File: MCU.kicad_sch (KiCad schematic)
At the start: 41 parts, among them IC9 ATSAMD21G18A-MF, J10 SAMTEC_SSW-106-01-L-S, J7 SAMTEC_SSW-108-01-G-S, J8 SAMTEC_SSW-110-01-G-S, J9 SAMTEC_SSW-108-01-G-S, Q1 XTAL_32.768KHZ_ABRACON_ABS09-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

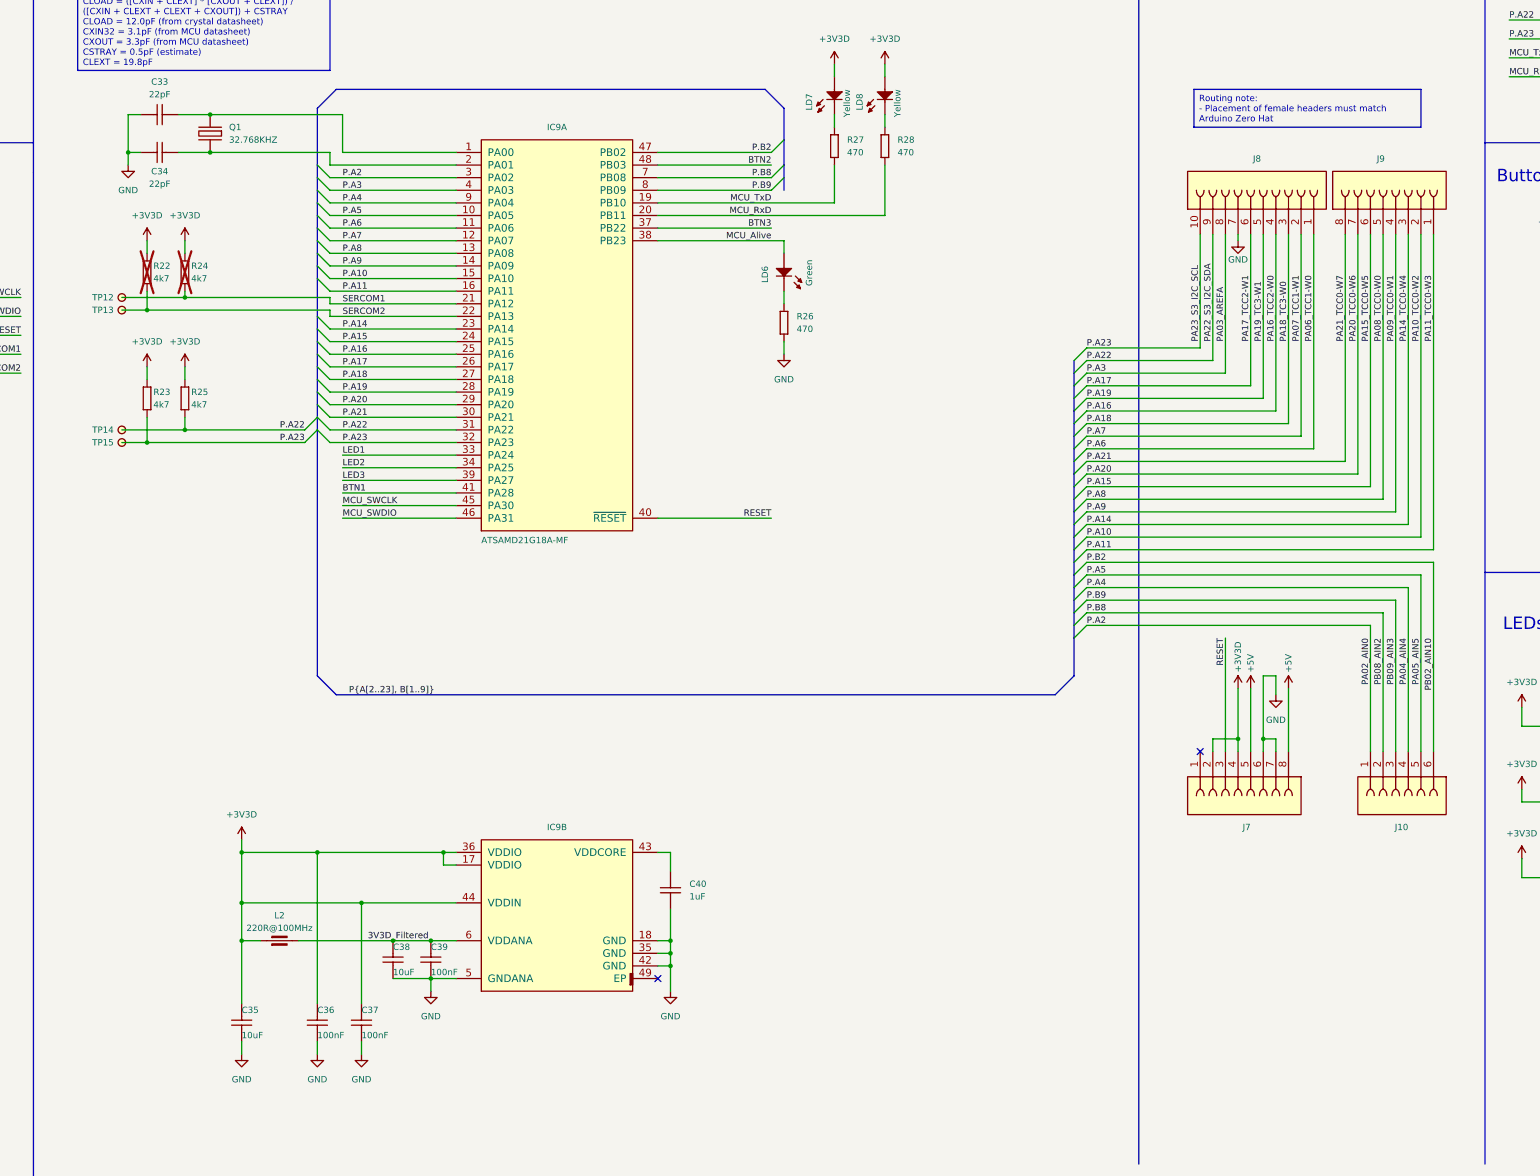
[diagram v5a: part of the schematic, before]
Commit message: Fixed reset circuits, removed 1V2 LED, fixing 2V5 circuit, added pullups to FPGA I2C, moved PSU TPs and JMPrs, replaced OSC2, removed ADC, added 2232 DTR, removed PSU seq TPs, replaced 2V5 LED res
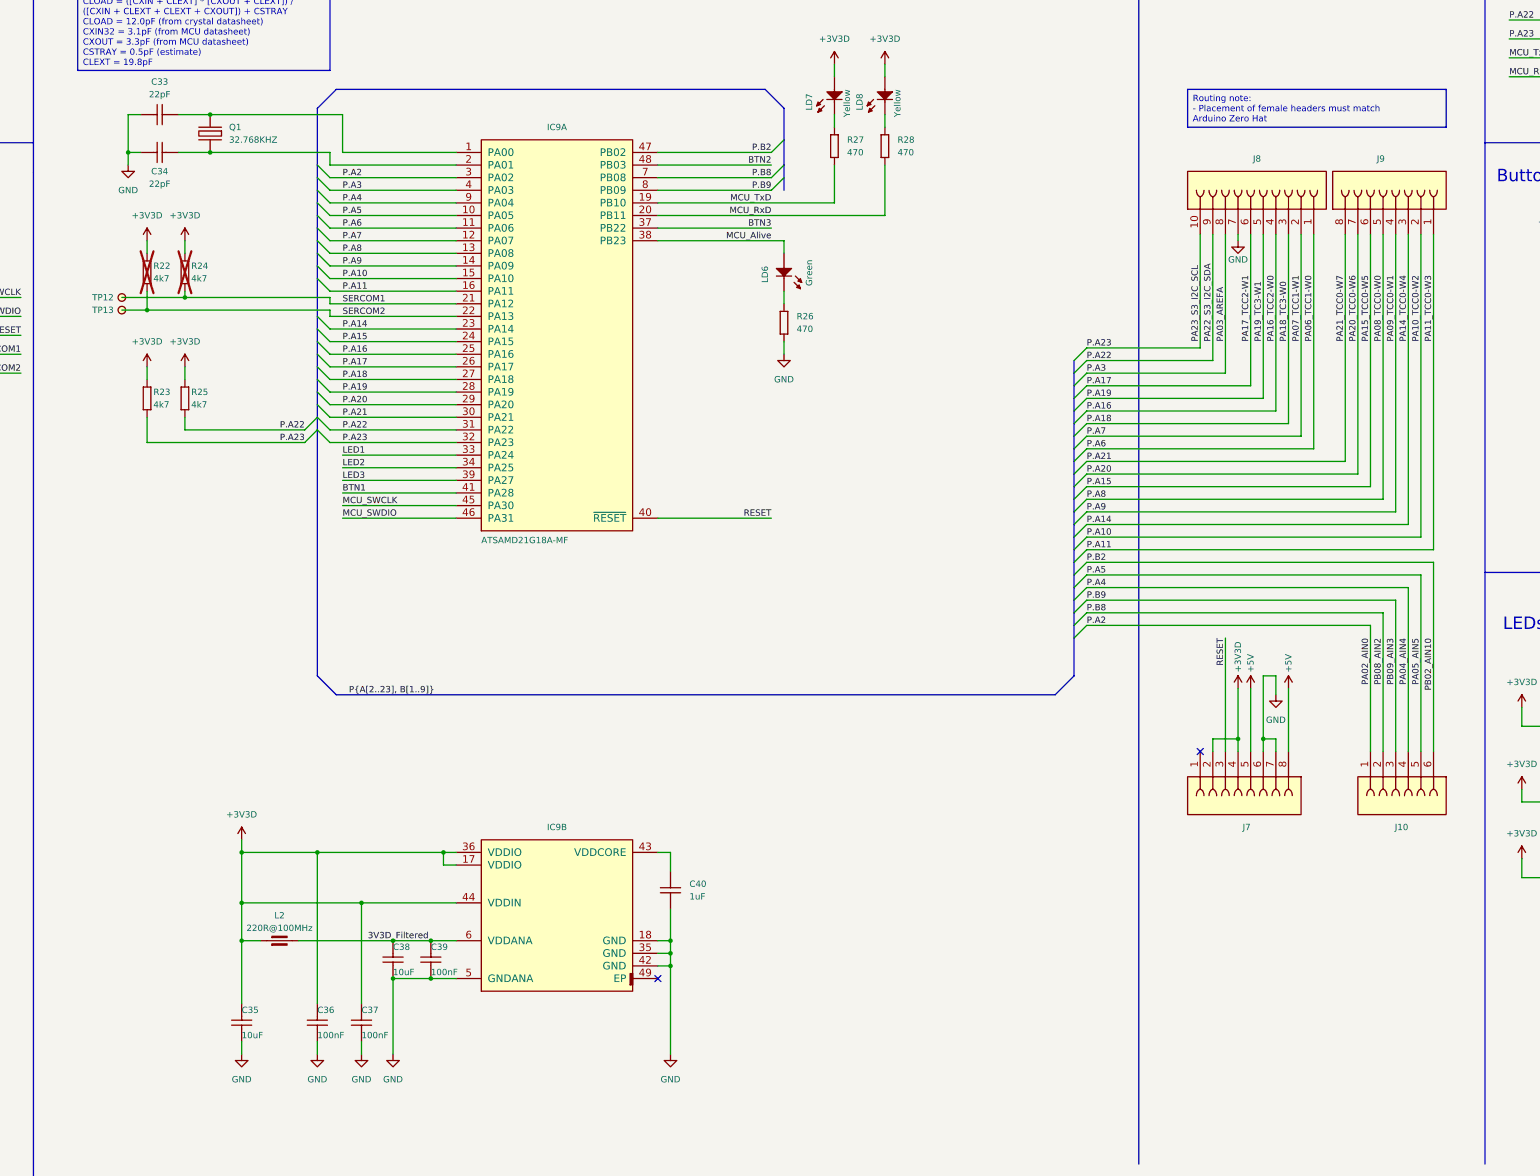
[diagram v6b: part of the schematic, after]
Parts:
- removed TP14, TP15: HARWIN_S1751-46, HARWIN SMD:HARWIN_S1751-46, symbol HARWIN:HARWIN_S1751-46

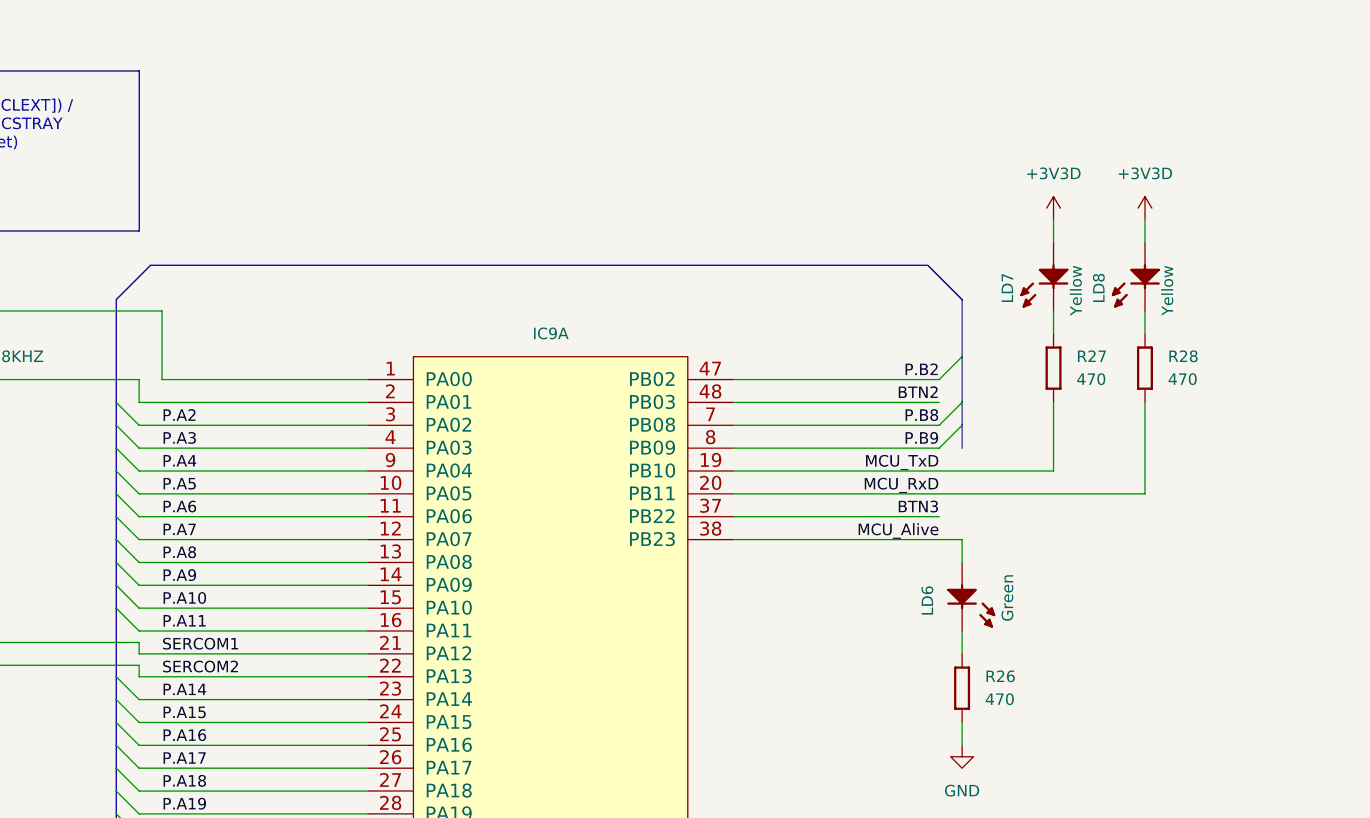
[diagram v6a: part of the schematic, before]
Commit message: Added circuit to turn on 1V2 LED, connected RX/TX LEDs to FT2232, moved PSU test points to before 0R res
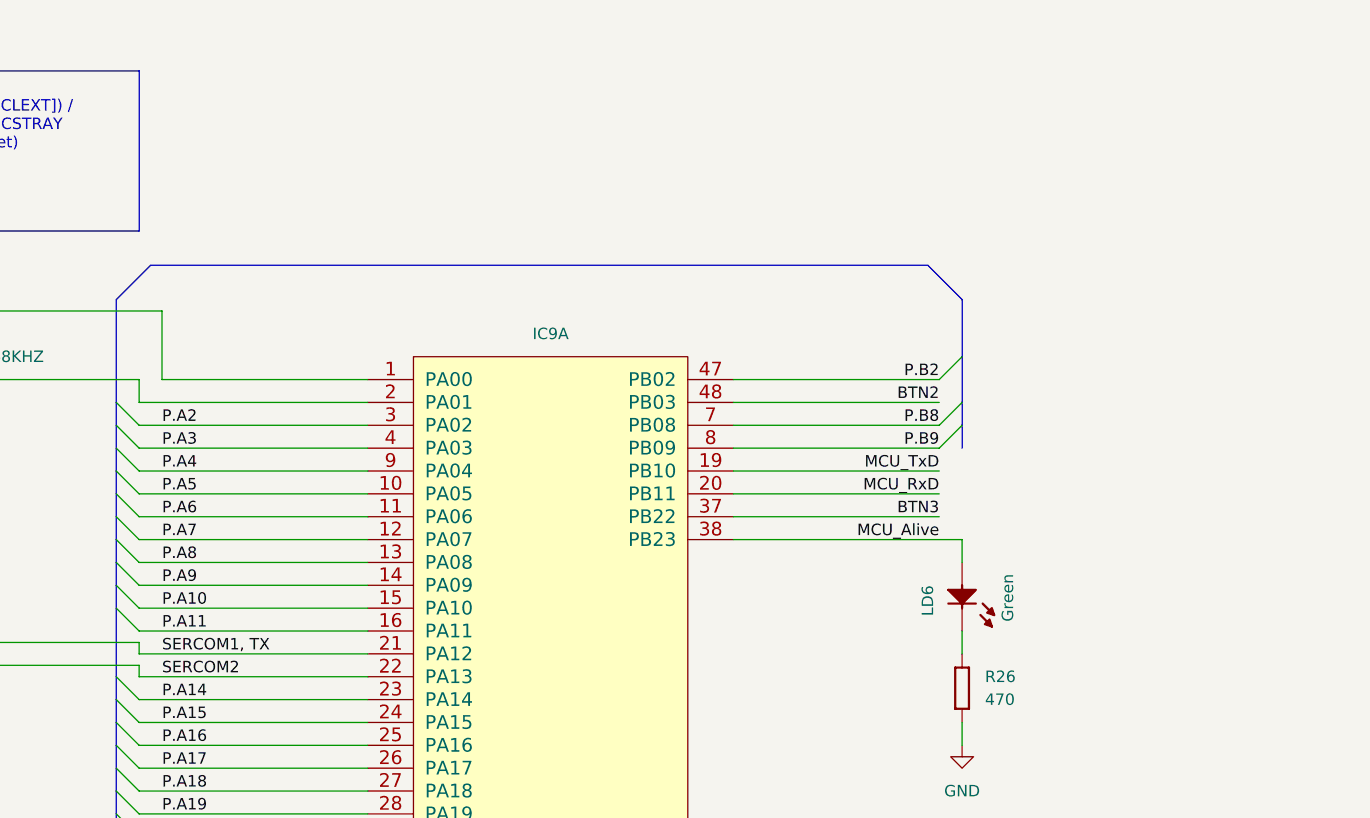
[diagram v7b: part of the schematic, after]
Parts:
- removed LD7, LD8: LED_LITEON_LTST-C193KSKT-5A, ICs And Semiconductors SMD:LED_LITEON_LTST-C193KSKT-5A, symbol LEDs & Displays:LED_LITEON_LTST-C193KSKT-5A
- removed R27, R28: R0603_470R_1%_0.1W_100PPM, Resistors SMD:RESC1608X55N, symbol Resistors SMD:R0603_470R_1%_0.1W_100PPM
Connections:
- net SERCOM1: no longer IC9.21 (PA12), R24.1, TP12.1
- new net SERCOM1, TX: IC9.21 (PA12), R24.1, TP12.1

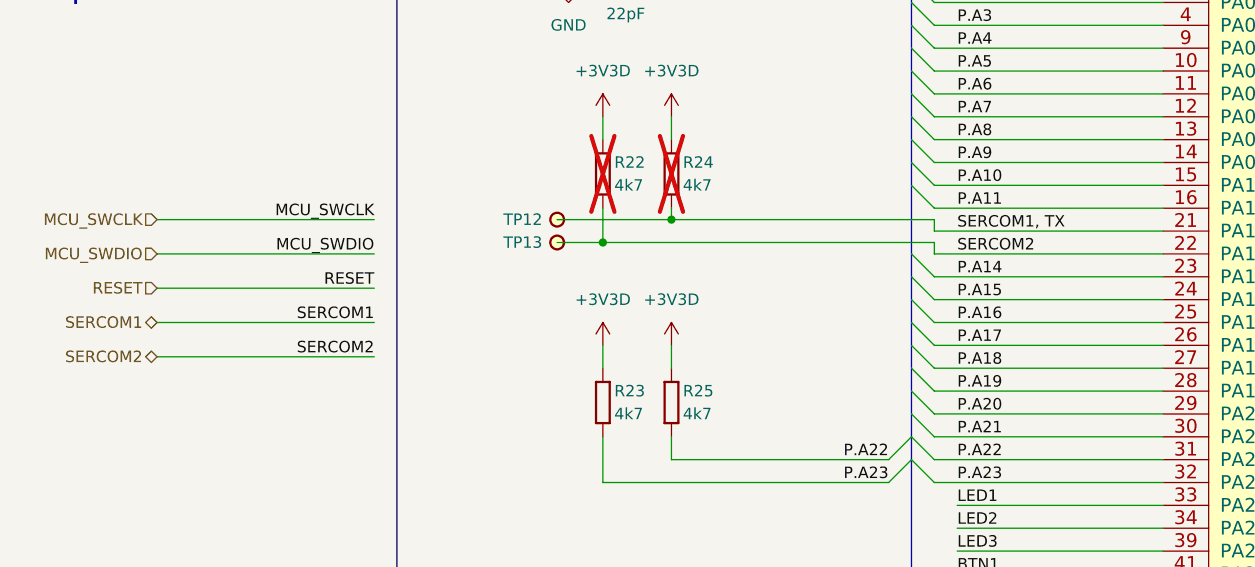
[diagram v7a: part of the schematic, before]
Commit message: Added FPGA reset button, renamed SERCOM
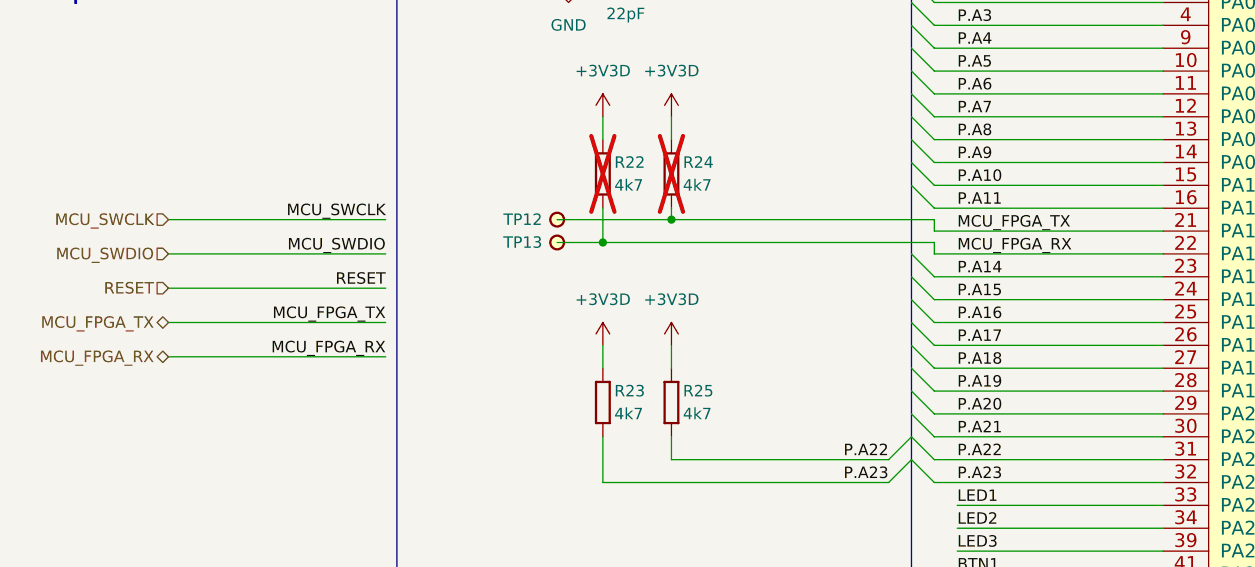
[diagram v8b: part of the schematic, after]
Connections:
- net SERCOM1, TX renamed MCU_FPGA_TX
- net SERCOM2 renamed MCU_FPGA_RX
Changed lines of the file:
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@@
 	(wire
 		(pts
-			(xy 26.67 88.9) (xy 50.8 88.9)
+			(xy 27.94 88.9) (xy 52.07 88.9)
 		)
 		(stroke
@@
 	(wire
 		(pts
-			(xy 26.67 100.33) (xy 50.8 100.33)
+			(xy 27.94 100.33) (xy 52.07 100.33)
 		)
 		(stroke
@@
 	(wire
 		(pts
-			(xy 26.67 96.52) (xy 50.8 96.52)
+			(xy 27.94 96.52) (xy 52.07 96.52)
 		)
 		(stroke
@@
 	(wire
 		(pts
-			(xy 26.67 92.71) (xy 50.8 92.71)
+			(xy 27.94 92.71) (xy 52.07 92.71)
 		)
 		(stroke
@@
 	(wire
 		(pts
-			(xy 26.67 85.09) (xy 50.8 85.09)
+			(xy 27.94 85.09) (xy 52.07 85.09)
 		)
 		(stroke
@@
 		)
 	)
-	(label "SERCOM2"
+	(label "MCU_FPGA_RX"
 		(at 115.57 88.9 0)
 		(fields_autoplaced yes)
@@
 	)
 	(label "MCU_SWCLK"
-		(at 50.8 85.09 180)
+		(at 52.07 85.09 180)
 		(fields_autoplaced yes)
 		(effects
@@
 		)
 	)
-	(label "SERCOM1"
-		(at 50.8 96.52 180)
-		(fields_autoplaced yes)
-		(effects
-			(font
-				(size 1.27 1.27)
-			)
-			(justify right bottom)
-		)
-	)
 	(label "PA06_TCC1-W0"
 		(at 311.15 93.98 90)
@@
 		)
 	)
-	(label "SERCOM2"
-		(at 50.8 100.33 180)
-		(fields_autoplaced yes)
-		(effects
-			(font
-				(size 1.27 1.27)
-			)
-			(justify right bottom)
-		)
-	)
 	(label "RESET"
 		(at 293.37 153.67 270)
@@
 		)
 	)
+	(label "MCU_FPGA_RX"
+		(at 52.07 100.33 180)
+		(fields_autoplaced yes)
+		(effects
+			(font
+				(size 1.27 1.27)
+			)
+			(justify right bottom)
+		)
+	)
 	(label "PB08_AIN2"
 		(at 325.12 153.67 270)
@@
 	)
 	(label "RESET"
-		(at 50.8 92.71 180)
+		(at 52.07 92.71 180)
 		(fields_autoplaced yes)
 		(effects
@@
 		)
 	)
+	(label "MCU_FPGA_TX"
+		(at 52.07 96.52 180)
+		(fields_autoplaced yes)
+		(effects
+			(font
+				(size 1.27 1.27)
+			)
+			(justify right bottom)
+		)
+	)
 	(label "P.A10"
 		(at 265.43 133.35 0)
@@
 	)
 	(label "MCU_SWDIO"
-		(at 50.8 88.9 180)
+		(at 52.07 88.9 180)
 		(fields_autoplaced yes)
 		(effects
@@
 		)
 	)
-	(label "SERCOM1, TX"
+	(label "MCU_FPGA_TX"
 		(at 115.57 86.36 0)
 		(fields_autoplaced yes)
@@
 	(hierarchical_label "MCU_SWDIO"
 		(shape input)
-		(at 26.67 88.9 180)
+		(at 27.94 88.9 180)
 		(fields_autoplaced yes)
 		(effects
@@
 	(hierarchical_label "RESET"
 		(shape input)
-		(at 26.67 92.71 180)
+		(at 27.94 92.71 180)
 		(fields_autoplaced yes)
 		(effects
@@
 	(hierarchical_label "MCU_SWCLK"
 		(shape input)
-		(at 26.67 85.09 180)
+		(at 27.94 85.09 180)
 		(fields_autoplaced yes)
 		(effects
@@
 		)
 	)
-	(hierarchical_label "SERCOM1"
+	(hierarchical_label "MCU_FPGA_TX"
 		(shape bidirectional)
-		(at 26.67 96.52 180)
+		(at 27.94 96.52 180)
 		(fields_autoplaced yes)
 		(effects
@@
 		)
 	)
-	(hierarchical_label "SERCOM2"
+	(hierarchical_label "MCU_FPGA_RX"
 		(shape bidirectional)
-		(at 26.67 100.33 180)
+		(at 27.94 100.33 180)
 		(fields_autoplaced yes)
 		(effects
